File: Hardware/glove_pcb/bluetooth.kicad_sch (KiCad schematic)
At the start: 12 parts, among them J13 Conn_01x01

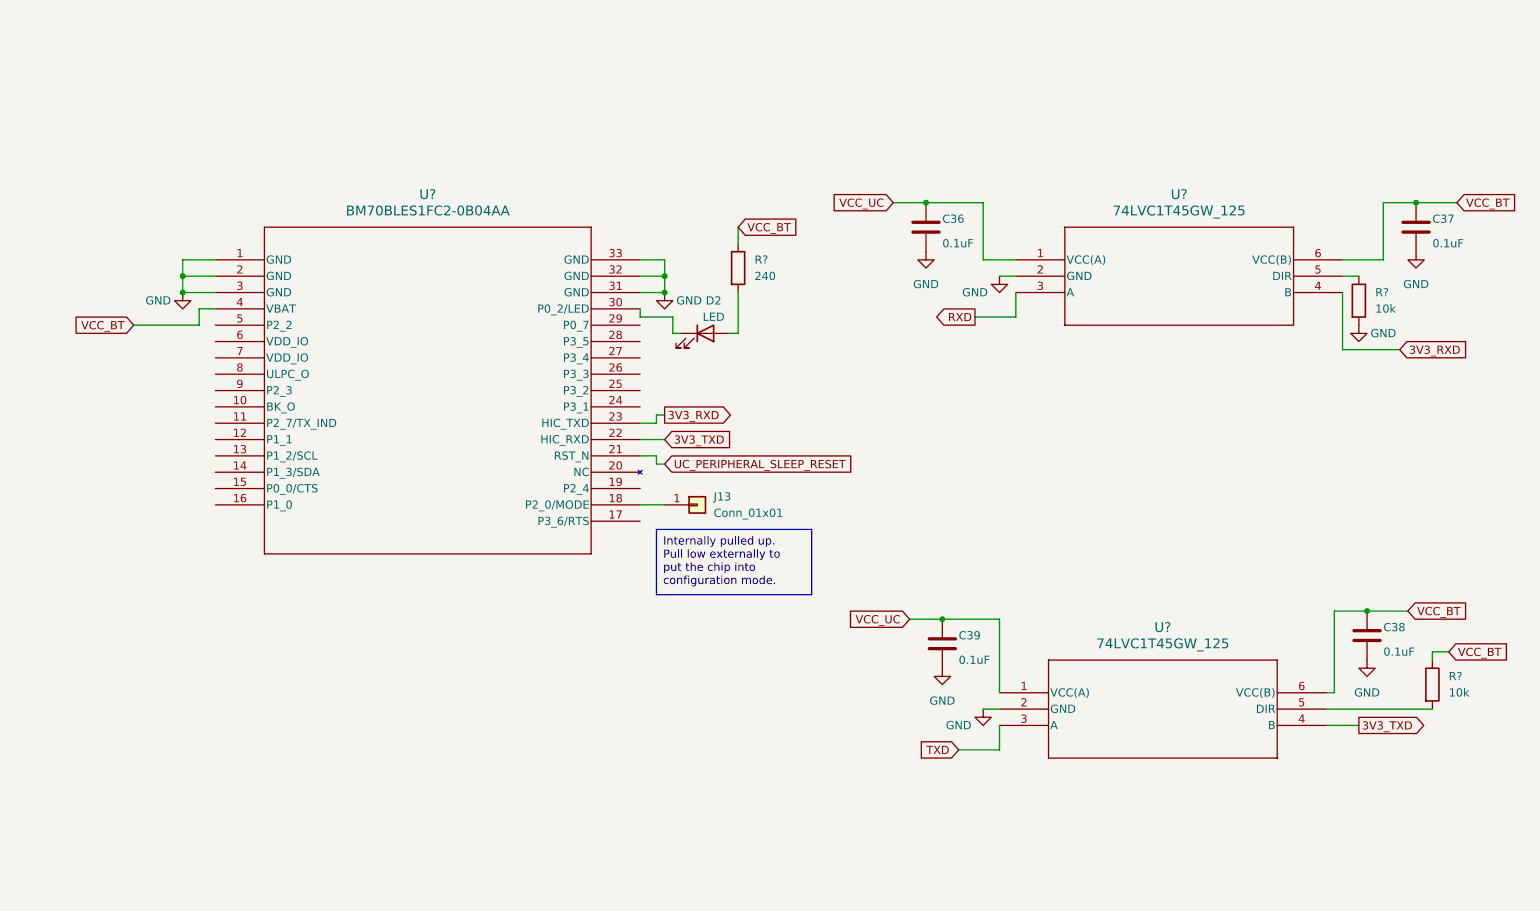
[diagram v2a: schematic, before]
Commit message: Added Footprints
I Added footprints for every components in PCB
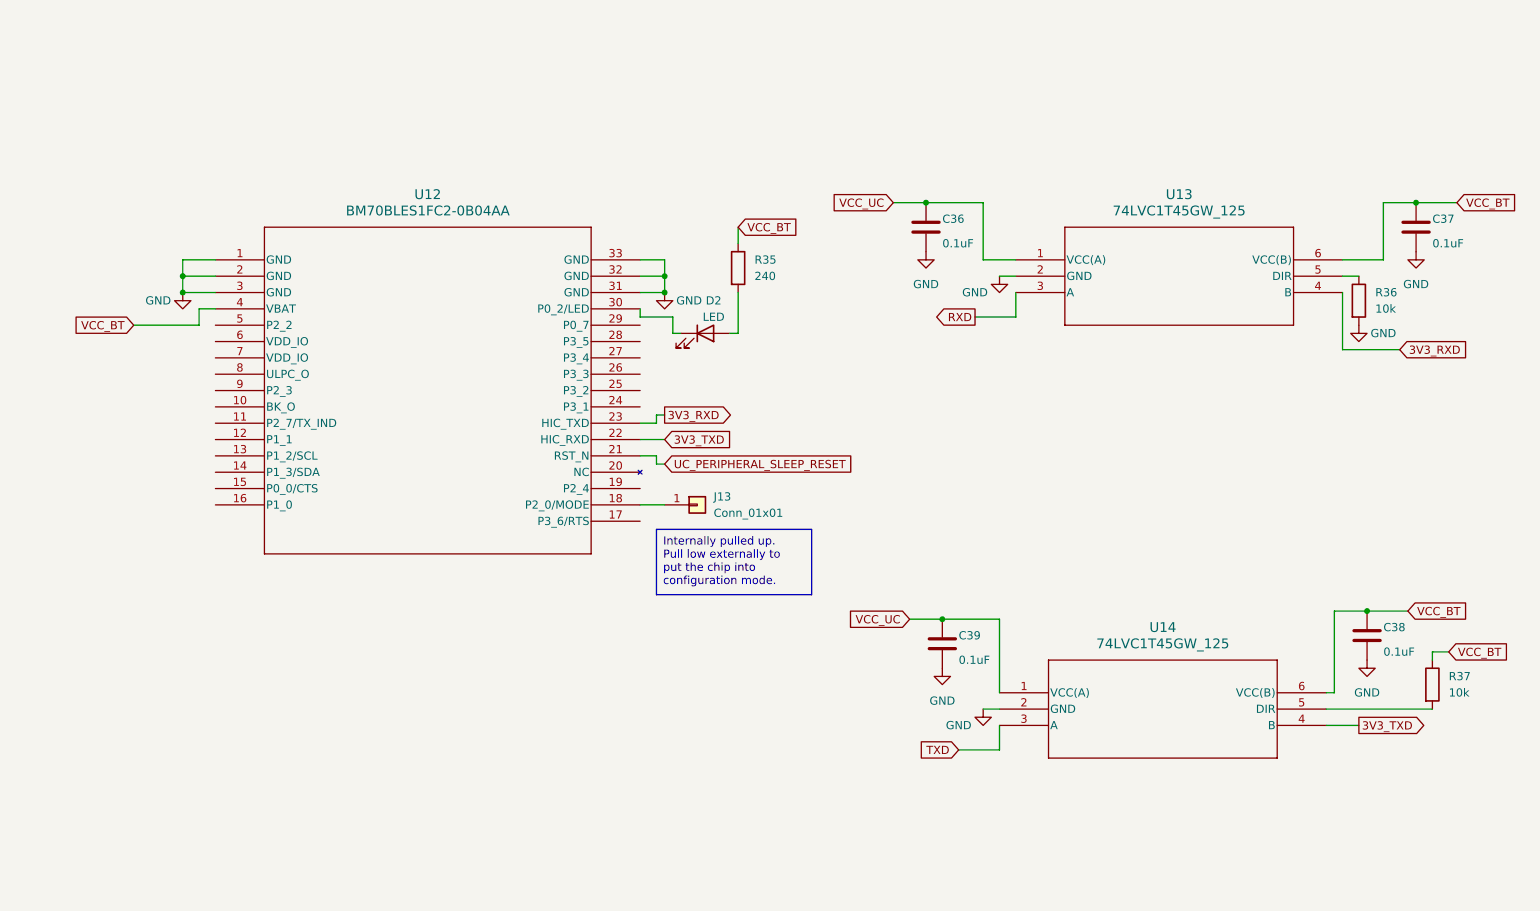
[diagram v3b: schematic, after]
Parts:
- C36, C37, C38, C39: footprint (none) -> Capacitor_SMD:C_0603_1608Metric_Pad1.08x0.95mm_HandSolder
- D2: footprint (none) -> LED_THT:LED_D5.0mm
- J13: footprint (none) -> Connector_PinSocket_2.54mm:PinSocket_1x01_P2.54mm_Vertical
- R35, R36, R37: renamed from R?; footprint (none) -> Resistor_SMD:R_0805_2012Metric_Pad1.20x1.40mm_HandSolder
- gave numbers to parts that had none: 3
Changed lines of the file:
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@@
       (effects (font (size 1.27 1.27)) (justify left))
     )
-    (property "Footprint" "" (at 169.8752 57.15 0)
+    (property "Footprint" "Capacitor_SMD:C_0603_1608Metric_Pad1.08x0.95mm_HandSolder" (at 169.8752 57.15 0)
       (effects (font (size 1.27 1.27)) hide)
     )
@@
       (effects (font (size 1.27 1.27)) (justify left))
     )
-    (property "Footprint" "" (at 238.4552 120.65 0)
+    (property "Footprint" "Capacitor_SMD:C_0603_1608Metric_Pad1.08x0.95mm_HandSolder" (at 238.4552 120.65 0)
       (effects (font (size 1.27 1.27)) hide)
     )
@@
   (symbol (lib_id "power:GND") (at 177.8 128.27 0) (unit 1)
     (in_bom yes) (on_board yes) (dnp no)
-    (property "Reference" "#PWR?" (at 177.8 134.62 0)
+    (property "Reference" "#PWR062" (at 177.8 134.62 0)
       (effects (font (size 1.27 1.27)) hide)
     )
@@
     (instances
       (project "glove_pcb"
-        (path "/747ff5f3-d342-40b0-8e4e-75b3a3063e75/ecec443b-784e-4f7b-9f78-072e3afadba0"
-          (reference "#PWR?") (unit 1)
-        )
         (path "/747ff5f3-d342-40b0-8e4e-75b3a3063e75/cc511a49-678e-4f62-8b05-bdef2fe6dbf9"
           (reference "#PWR062") (unit 1)
@@
   (symbol (lib_id "Glove_Symbols:74LVC1T45GW_125") (at 180.34 125.73 0) (unit 1)
     (in_bom yes) (on_board yes) (dnp no) (fields_autoplaced)
-    (property "Reference" "U?" (at 205.74 115.57 0)
+    (property "Reference" "U14" (at 205.74 115.57 0)
       (effects (font (size 1.524 1.524)))
     )
@@
     (instances
       (project "glove_pcb"
-        (path "/747ff5f3-d342-40b0-8e4e-75b3a3063e75/ecec443b-784e-4f7b-9f78-072e3afadba0"
-          (reference "U?") (unit 1)
-        )
         (path "/747ff5f3-d342-40b0-8e4e-75b3a3063e75/cc511a49-678e-4f62-8b05-bdef2fe6dbf9"
           (reference "U14") (unit 1)
@@
       (effects (font (size 1.27 1.27)) (justify left))
     )
-    (property "Footprint" "" (at 172.4152 121.92 0)
+    (property "Footprint" "Capacitor_SMD:C_0603_1608Metric_Pad1.08x0.95mm_HandSolder" (at 172.4152 121.92 0)
       (effects (font (size 1.27 1.27)) hide)
     )
@@
   (symbol (lib_id "Device:R") (at 236.22 64.77 0) (unit 1)
     (in_bom yes) (on_board yes) (dnp no) (fields_autoplaced)
-    (property "Reference" "R?" (at 238.76 63.5 0)
+    (property "Reference" "R36" (at 238.76 63.5 0)
       (effects (font (size 1.27 1.27)) (justify left))
     )
@@
       (effects (font (size 1.27 1.27)) (justify left))
     )
-    (property "Footprint" "" (at 234.442 64.77 90)
+    (property "Footprint" "Resistor_SMD:R_0805_2012Metric_Pad1.20x1.40mm_HandSolder" (at 234.442 64.77 90)
       (effects (font (size 1.27 1.27)) hide)
     )
@@
     (instances
       (project "glove_pcb"
-        (path "/747ff5f3-d342-40b0-8e4e-75b3a3063e75/ecec443b-784e-4f7b-9f78-072e3afadba0"
-          (reference "R?") (unit 1)
-        )
         (path "/747ff5f3-d342-40b0-8e4e-75b3a3063e75/cc511a49-678e-4f62-8b05-bdef2fe6dbf9"
           (reference "R36") (unit 1)
@@
   (symbol (lib_id "power:GND") (at 180.34 60.96 0) (unit 1)
     (in_bom yes) (on_board yes) (dnp no)
-    (property "Reference" "#PWR?" (at 180.34 67.31 0)
+    (property "Reference" "#PWR057" (at 180.34 67.31 0)
       (effects (font (size 1.27 1.27)) hide)
     )
@@
     (instances
       (project "glove_pcb"
-        (path "/747ff5f3-d342-40b0-8e4e-75b3a3063e75/ecec443b-784e-4f7b-9f78-072e3afadba0"
-          (reference "#PWR?") (unit 1)
-        )
         (path "/747ff5f3-d342-40b0-8e4e-75b3a3063e75/cc511a49-678e-4f62-8b05-bdef2fe6dbf9"
           (reference "#PWR057") (unit 1)
@@
       (effects (font (size 1.27 1.27)))
     )
-    (property "Footprint" "" (at 134.62 69.85 0)
+    (property "Footprint" "LED_THT:LED_D5.0mm" (at 134.62 69.85 0)
       (effects (font (size 1.27 1.27)) hide)
     )
@@
   (symbol (lib_id "Device:R") (at 247.65 124.46 0) (unit 1)
     (in_bom yes) (on_board yes) (dnp no) (fields_autoplaced)
-    (property "Reference" "R?" (at 250.19 123.19 0)
+    (property "Reference" "R37" (at 250.19 123.19 0)
       (effects (font (size 1.27 1.27)) (justify left))
     )
@@
       (effects (font (size 1.27 1.27)) (justify left))
     )
-    (property "Footprint" "" (at 245.872 124.46 90)
+    (property "Footprint" "Resistor_SMD:R_0805_2012Metric_Pad1.20x1.40mm_HandSolder" (at 245.872 124.46 90)
       (effects (font (size 1.27 1.27)) hide)
     )
@@
     (instances
       (project "glove_pcb"
-        (path "/747ff5f3-d342-40b0-8e4e-75b3a3063e75/ecec443b-784e-4f7b-9f78-072e3afadba0"
-          (reference "R?") (unit 1)
-        )
         (path "/747ff5f3-d342-40b0-8e4e-75b3a3063e75/cc511a49-678e-4f62-8b05-bdef2fe6dbf9"
           (reference "R37") (unit 1)
@@
       (effects (font (size 1.27 1.27)) (justify left))
     )
-    (property "Footprint" "" (at 133.35 96.52 0)
+    (property "Footprint" "Connector_PinSocket_2.54mm:PinSocket_1x01_P2.54mm_Vertical" (at 133.35 96.52 0)
       (effects (font (size 1.27 1.27)) hide)
     )
@@
       (effects (font (size 1.27 1.27)) (justify left))
     )
-    (property "Footprint" "" (at 246.0752 57.15 0)
+    (property "Footprint" "Capacitor_SMD:C_0603_1608Metric_Pad1.08x0.95mm_HandSolder" (at 246.0752 57.15 0)
       (effects (font (size 1.27 1.27)) hide)
     )
@@
   (symbol (lib_id "Glove_Symbols:BM70BLES1FC2-0B04AA") (at 58.42 58.42 0) (unit 1)
     (in_bom yes) (on_board yes) (dnp no) (fields_autoplaced)
-    (property "Reference" "U?" (at 91.44 48.26 0)
+    (property "Reference" "U12" (at 91.44 48.26 0)
       (effects (font (size 1.524 1.524)))
     )
@@
     (instances
       (project "glove_pcb"
-        (path "/747ff5f3-d342-40b0-8e4e-75b3a3063e75/ecec443b-784e-4f7b-9f78-072e3afadba0"
-          (reference "U?") (unit 1)
-        )
         (path "/747ff5f3-d342-40b0-8e4e-75b3a3063e75/cc511a49-678e-4f62-8b05-bdef2fe6dbf9"
           (reference "U12") (unit 1)
@@
   (symbol (lib_id "Glove_Symbols:74LVC1T45GW_125") (at 182.88 58.42 0) (unit 1)
     (in_bom yes) (on_board yes) (dnp no) (fields_autoplaced)
-    (property "Reference" "U?" (at 208.28 48.26 0)
+    (property "Reference" "U13" (at 208.28 48.26 0)
       (effects (font (size 1.524 1.524)))
     )
@@
     (instances
       (project "glove_pcb"
-        (path "/747ff5f3-d342-40b0-8e4e-75b3a3063e75/ecec443b-784e-4f7b-9f78-072e3afadba0"
-          (reference "U?") (unit 1)
-        )
         (path "/747ff5f3-d342-40b0-8e4e-75b3a3063e75/cc511a49-678e-4f62-8b05-bdef2fe6dbf9"
           (reference "U13") (unit 1)
@@
   (symbol (lib_id "Device:R") (at 139.7 59.69 0) (unit 1)
     (in_bom yes) (on_board yes) (dnp no) (fields_autoplaced)
-    (property "Reference" "R?" (at 142.24 58.42 0)
+    (property "Reference" "R35" (at 142.24 58.42 0)
       (effects (font (size 1.27 1.27)) (justify left))
     )
@@
       (effects (font (size 1.27 1.27)) (justify left))
     )
-    (property "Footprint" "" (at 137.922 59.69 90)
+    (property "Footprint" "Resistor_SMD:R_0805_2012Metric_Pad1.20x1.40mm_HandSolder" (at 137.922 59.69 90)
       (effects (font (size 1.27 1.27)) hide)
     )
@@
     (instances
       (project "glove_pcb"
-        (path "/747ff5f3-d342-40b0-8e4e-75b3a3063e75/ecec443b-784e-4f7b-9f78-072e3afadba0"
-          (reference "R?") (unit 1)
-        )
         (path "/747ff5f3-d342-40b0-8e4e-75b3a3063e75/cc511a49-678e-4f62-8b05-bdef2fe6dbf9"
           (reference "R35") (unit 1)
@@
   (symbol (lib_id "power:GND") (at 236.22 68.58 0) (unit 1)
     (in_bom yes) (on_board yes) (dnp no)
-    (property "Reference" "#PWR?" (at 236.22 74.93 0)
+    (property "Reference" "#PWR059" (at 236.22 74.93 0)
       (effects (font (size 1.27 1.27)) hide)
     )
@@
     (instances
       (project "glove_pcb"
-        (path "/747ff5f3-d342-40b0-8e4e-75b3a3063e75/ecec443b-784e-4f7b-9f78-072e3afadba0"
-          (reference "#PWR?") (unit 1)
-        )
         (path "/747ff5f3-d342-40b0-8e4e-75b3a3063e75/cc511a49-678e-4f62-8b05-bdef2fe6dbf9"
           (reference "#PWR059") (unit 1)

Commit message: Made most of changes from meeting
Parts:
- removed J13: Conn_01x01, Connector_PinSocket_2.54mm:PinSocket_1x01_P2.54mm_Vertical, symbol Connector_Generic:Conn_01x01
- added C40, C41: 0.1uF, Capacitor_SMD:C_0603_1608Metric_Pad1.08x0.95mm_HandSolder, symbol Device:C
- added JP1: Jumper_2_Open, symbol Jumper:Jumper_2_Open
- added U15: 74LVC1T45GW_125, TSSOP6_SOT363-2_NEX, symbol Glove_Symbols:74LVC1T45GW_125
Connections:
- net VCC_UC is gone; now on net +5V: C36.1, C39.1, U13.1 (VCC(A)), U14.1 (VCC(A))
- net GND: now also U13.5 (DIR), C40.2, C41.2, JP1.2 (B), U15.2 (GND); no longer R36.2
- net UC_PERIPHERAL_SLEEP_RESET: now also U15.3 (A); no longer U12.21 (RST_N)
- net +5V: now reaches R36.1
- net +5V: now also R37.1, C40.1, U15.1 (VCC(A)); no longer U13.5 (DIR)
- net at U12.18 (P2_0/MODE): now also JP1.1 (A)
- net VCC_BT renamed +3.3V
- net +3.3V: now also C41.1, U15.6 (VCC(B)); no longer R37.1
- new net: R36.2, U15.5 (DIR)
- new net 3V3_UC_PERIPHERAL_SLEEP_RESET: U12.21 (RST_N), U15.4 (B)
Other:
- moved on the sheet: C36, C37, C38, C39, D2, R35, R37, U12, U13, U14

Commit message: Finish changes according to feedback
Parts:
- removed C40, C41: 0.1uF, Capacitor_SMD:C_0603_1608Metric_Pad1.08x0.95mm_HandSolder, symbol Device:C
- removed R36: 10k, Resistor_SMD:R_0805_2012Metric_Pad1.20x1.40mm_HandSolder, symbol Device:R
- removed U15: 74LVC1T45GW_125, TSSOP6_SOT363-2_NEX, symbol Glove_Symbols:74LVC1T45GW_125
- added R32: 10k, Resistor_SMD:R_0805_2012Metric_Pad1.20x1.40mm_HandSolder, symbol Device:R
- added U13: MCP111T-195I/TT, SOT-23_MC_MCH, symbol Glove_Symbols:MCP111T-195I_TT
- renumbered C38 to C52, C36 to C53, C37 to C54, C39 to C55, R35 to R31, R37 to R33, U13 to U14, U14 to U15
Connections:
- net +3.3V: now also R32.1, U13.3 (VDD)
- net GND: now also U13.2 (VSS)
- net 3V3_UC_PERIPHERAL_SLEEP_RESET: no longer names the net of U12.21 (RST_N)
- net 3V3_UC_PERIPHERAL_SLEEP_RESET: now also R32.2, U13.1 (VOUT)

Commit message: Finish schematic updates
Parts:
- renumbered U12 to U16, U13 to U17, U14 to U18, U15 to U19

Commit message: Change isp pin symbol
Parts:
- U16: footprint BM70BLES1FC2_MCH -> Glove_Footprints:BM70BLES1FC2_MCH
- U17: footprint SOT-23_MC_MCH -> Glove_Footprints:SOT-23_MC_MCH
- U18, U19: footprint TSSOP6_SOT363-2_NEX -> Glove_Footprints:TSSOP6_SOT363-2_NEX
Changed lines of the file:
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@@
       (effects (font (size 1.524 1.524)))
     )
-    (property "Footprint" "TSSOP6_SOT363-2_NEX" (at 161.29 109.22 0)
+    (property "Footprint" "Glove_Footprints:TSSOP6_SOT363-2_NEX" (at 161.29 109.22 0)
       (effects (font (size 1.27 1.27) italic) hide)
     )
@@
       (effects (font (size 1.524 1.524)))
     )
-    (property "Footprint" "BM70BLES1FC2_MCH" (at 46.99 31.75 0)
+    (property "Footprint" "Glove_Footprints:BM70BLES1FC2_MCH" (at 46.99 31.75 0)
       (effects (font (size 1.27 1.27) italic) hide)
     )
@@
       (effects (font (size 1.524 1.524)))
     )
-    (property "Footprint" "TSSOP6_SOT363-2_NEX" (at 50.8 106.68 0)
+    (property "Footprint" "Glove_Footprints:TSSOP6_SOT363-2_NEX" (at 50.8 106.68 0)
       (effects (font (size 1.27 1.27) italic) hide)
     )
@@
       (effects (font (size 1.524 1.524)))
     )
-    (property "Footprint" "SOT-23_MC_MCH" (at 137.16 62.23 0)
-      (effects (font (size 1.27 1.27) italic) hide)
-    )
+    (property "Footprint" "Glove_Footprints:SOT-23_MC_MCH" (at 137.16 62.23 0)
+      (effects (font (size 1.27 1.27) italic) hide)
+    )
